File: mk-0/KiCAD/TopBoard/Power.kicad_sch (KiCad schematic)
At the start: 33 parts, among them J3 USB_C_Receptacle_USB2.0_16P, J5 Raspberry_Pi_2_3, U10 SRV05-4, U11 AMS1117-1.2, U6 CAT24C256, U9 AMS1117-3.3

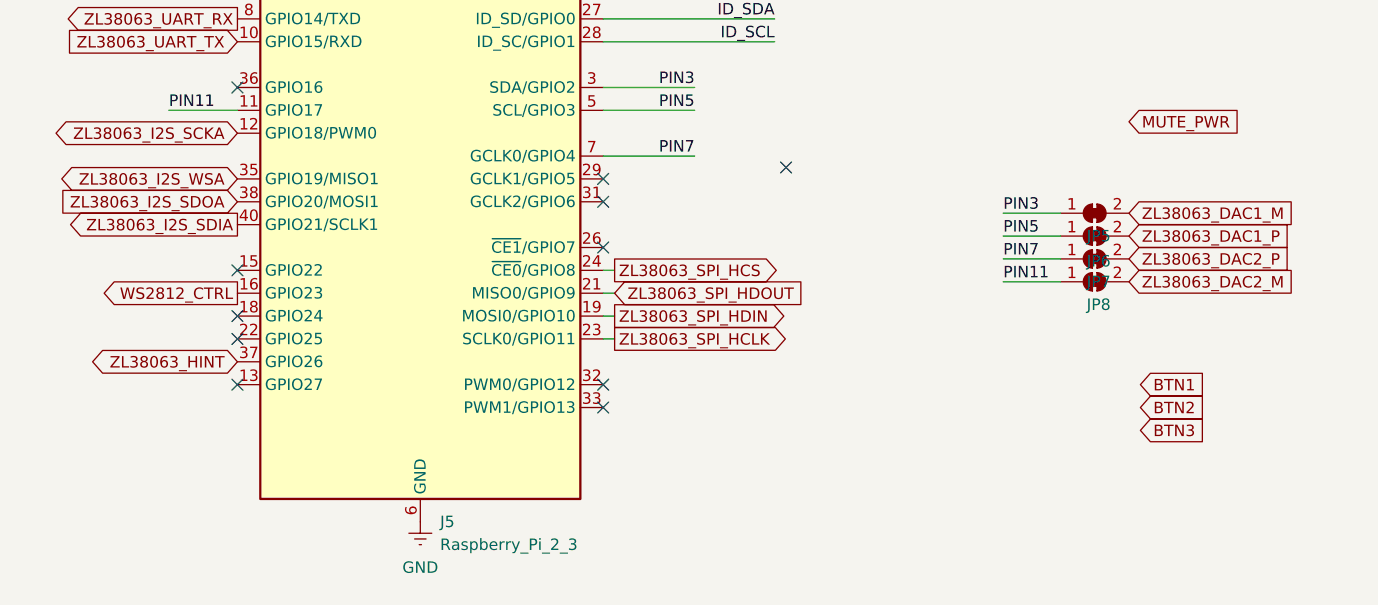
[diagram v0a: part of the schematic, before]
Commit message: Added 3.5mm Jack to top board
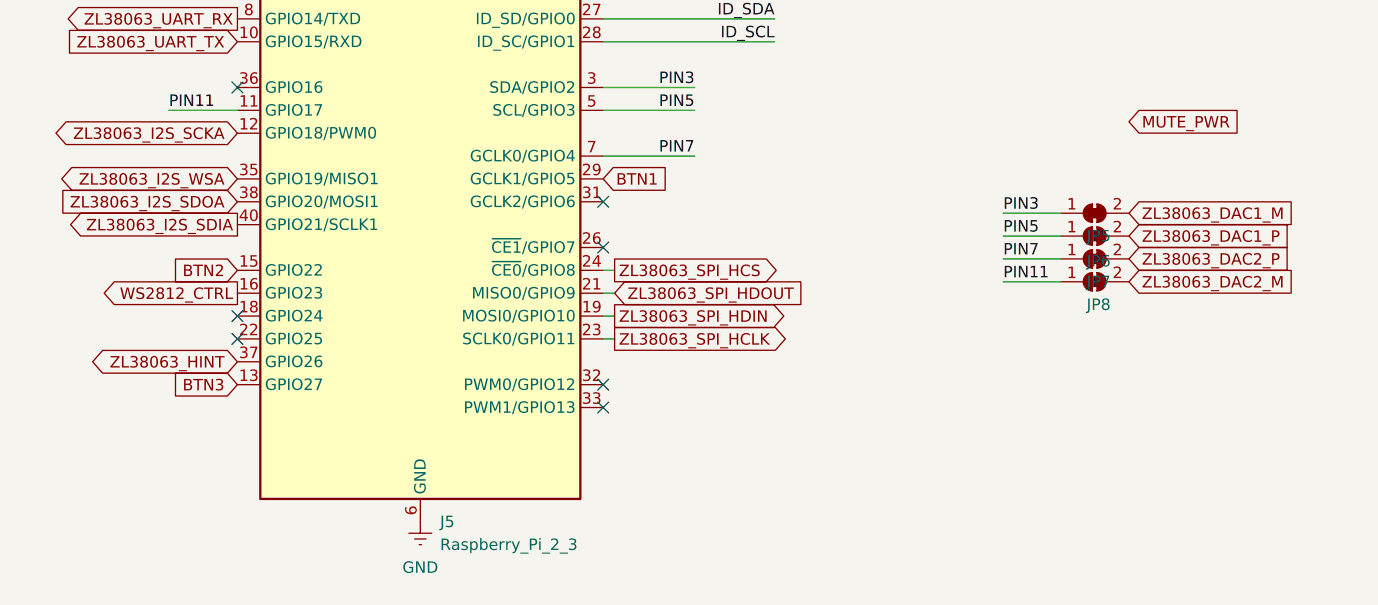
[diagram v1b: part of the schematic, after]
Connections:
- net BTN1: now also J5.29 (GCLK1/GPIO5)
- net BTN2: now also J5.15 (GPIO22)
- net BTN3: now also J5.13 (GPIO27)
- no-connect marks 19 -> 15
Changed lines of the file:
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@@
-	)
-	(no_connect
-		(at 36.83 66.04)
 	)
 	(no_connect
@@
 	)
 	(no_connect
-		(at 97.79 54.61)
+		(at 77.47 81.28)
 	)
 	(no_connect
@@
 	)
 	(no_connect
-		(at 77.47 55.88)
-	)
-	(no_connect
 		(at 77.47 58.42)
 	)
@@
 	)
 	(no_connect
-		(at 77.47 81.28)
-	)
-	(no_connect
 		(at 203.2 64.77)
 	)
@@
 	(no_connect
 		(at 69.85 177.8)
-	)
-	(no_connect
-		(at 36.83 78.74)
 	)
 	(no_connect
@@
 	(global_label "BTN1"
 		(shape input)
-		(at 137.16 78.74 0)
+		(at 77.47 55.88 0)
 		(fields_autoplaced yes)
 		(effects
@@
 		)
 		(property "Intersheetrefs" "${INTERSHEET_REFS}"
-			(at 145.0179 78.74 0)
+			(at 85.3279 55.88 0)
 			(effects
 				(font
@@
 	(global_label "BTN2"
 		(shape input)
-		(at 137.16 81.28 0)
-		(fields_autoplaced yes)
-		(effects
-			(font
-				(size 1.27 1.27)
-			)
-			(justify left)
+		(at 36.83 66.04 180)
+		(fields_autoplaced yes)
+		(effects
+			(font
+				(size 1.27 1.27)
+			)
+			(justify right)
 		)
 		(property "Intersheetrefs" "${INTERSHEET_REFS}"
-			(at 145.0179 81.28 0)
+			(at 28.9721 66.04 0)
 			(effects
 				(font
 					(size 1.27 1.27)
 				)
-				(justify left)
+				(justify right)
 				(hide yes)
 			)
@@
 	(global_label "BTN3"
 		(shape input)
-		(at 137.16 83.82 0)
-		(fields_autoplaced yes)
-		(effects
-			(font
-				(size 1.27 1.27)
-			)
-			(justify left)
+		(at 36.83 78.74 180)
+		(fields_autoplaced yes)
+		(effects
+			(font
+				(size 1.27 1.27)
+			)
+			(justify right)
 		)
 		(property "Intersheetrefs" "${INTERSHEET_REFS}"
-			(at 145.0179 83.82 0)
+			(at 28.9721 78.74 0)
 			(effects
 				(font
 					(size 1.27 1.27)
 				)
-				(justify left)
+				(justify right)
 				(hide yes)
 			)

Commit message: Cleanup and naming of Touchpoints
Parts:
- added TP13: GPIO7, TestPoint:TestPoint_Pad_D1.0mm, symbol Connector:TestPoint
- added TP14: GPIO12, TestPoint:TestPoint_Pad_D1.0mm, symbol Connector:TestPoint
- added TP15: GPIO16, TestPoint:TestPoint_Pad_D1.0mm, symbol Connector:TestPoint
- added TP16: GPIO24, TestPoint:TestPoint_Pad_D1.0mm, symbol Connector:TestPoint
- added TP17: GPIO25, TestPoint:TestPoint_Pad_D1.0mm, symbol Connector:TestPoint
- added TP9: GPIO6, TestPoint:TestPoint_Pad_D1.0mm, symbol Connector:TestPoint
- TP10: value TestPoint -> 1V2
- TP11: value TestPoint -> GND
- TP7: value TestPoint -> 3V3
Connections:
- net MUTE_PWR: now also J5.33 (PWM1/GPIO13)
- net at J5.18 (GPIO24): now also TP16.1
- net at J5.22 (GPIO25): now also TP17.1
- net at J5.26 (~{CE1}/GPIO7): now also TP13.1
- net at J5.31 (GCLK2/GPIO6): now also TP9.1
- net at J5.32 (PWM0/GPIO12): now also TP14.1
- net at J5.36 (GPIO16): now also TP15.1
- net PIN11: no longer names the net of J5.11 (GPIO17), JP8.1 (A)
- net PIN3: no longer names the net of J5.3 (SDA/GPIO2), JP5.1 (A)
- net PIN5: no longer names the net of J5.5 (SCL/GPIO3), JP6.1 (A)
- net PIN7: no longer names the net of J5.7 (GCLK0/GPIO4), JP7.1 (A)
- no-connect marks 15 -> 8
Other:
- note added: "40 Pin / RPi header"
- note added: "Power"
- note added: "RPi HAT ID EEPROM"
- note added: "USB for Debug/Stand alone use"
- moved on the sheet: C43, C44, C45, C46, C47, C48, C49, C51, C52, C8, D15, D16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
